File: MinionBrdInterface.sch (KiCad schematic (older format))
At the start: 8 parts, among them J7 MinionConn, U20 HX1188FNL, U5 LTC6820

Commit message: Lays out PCB for Controls leader board
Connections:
- net labels added: UART_Rx, UART_Tx
- net labels removed: UART2_Rx, UART2_Tx
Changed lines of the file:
@@
 $Descr A4 11693 8268
 encoding utf-8
-Sheet 10 11
+Sheet 10 10
 Title ""
 Date ""
@@
 Wire Wire Line
 	9750 3450 9400 3450
+Text Label 9400 3450 0    50   ~ 0
+UART_Rx
 Text Label 9400 3350 0    50   ~ 0
-UART2_Rx
-Text Label 9400 3450 0    50   ~ 0
-UART2_Tx
+UART_Tx
 Wire Wire Line
 	8350 3550 9750 3550
@@
 NoConn ~ 9750 4150
 NoConn ~ 9750 4250
-Text HLabel 9400 3350 0    50   Output ~ 0
-UART2_Rx
-Text HLabel 9400 3450 0    50   Input ~ 0
-UART2_Tx
+Text HLabel 9400 3450 0    50   Output ~ 0
+UART_Rx
+Text HLabel 9400 3350 0    50   Input ~ 0
+UART_Tx
+Text Label 2850 3700 0    50   ~ 0
+MOSI
+Text Label 2850 3800 0    50   ~ 0
+MISO
+Text Label 2850 3900 0    50   ~ 0
+CLK
+Text Label 2850 4000 0    50   ~ 0
+CS
 $EndSCHEMATC

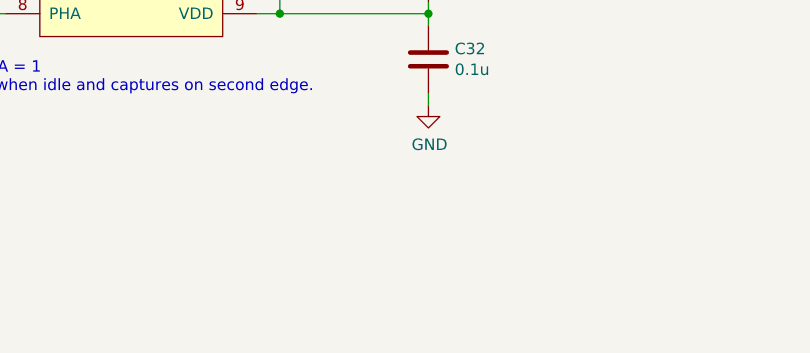
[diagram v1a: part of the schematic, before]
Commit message: Adds SPI header to test
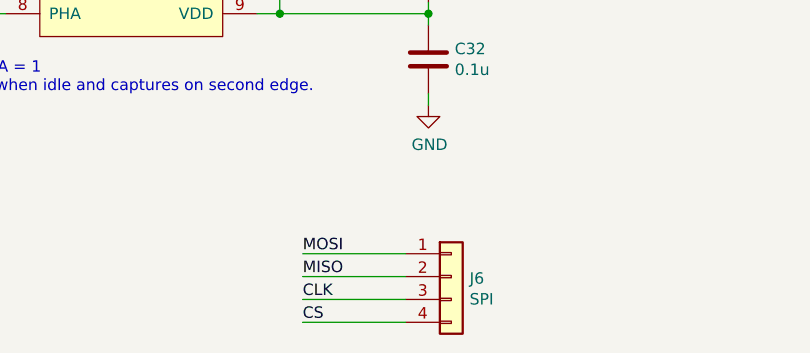
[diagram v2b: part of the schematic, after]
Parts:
- added J6: SPI, Connector_PinHeader_2.54mm:PinHeader_1x04_P2.54mm_Vertical, symbol Connector_Generic:Conn_01x04
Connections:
- wire segments 55 -> 59
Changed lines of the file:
@@
 Text Label 2850 4000 0    50   ~ 0
 CS
+$Comp
+L Connector_Generic:Conn_01x04 J6
+U 1 1 5F76763B
+P 5250 5450
+F 0 "J6" H 5330 5442 50  0000 L CNN
+F 1 "SPI" H 5330 5351 50  0000 L CNN
+F 2 "Connector_PinHeader_2.54mm:PinHeader_1x04_P2.54mm_Vertical" H 5250 5450 50  0001 C CNN
+F 3 "~" H 5250 5450 50  0001 C CNN
+	1    5250 5450
+	1    0    0    -1
+$EndComp
+Wire Wire Line
+	4600 5350 5050 5350
+Wire Wire Line
+	4600 5550 5050 5550
+Wire Wire Line
+	4600 5650 5050 5650
+Wire Wire Line
+	4600 5450 5050 5450
+Text Label 4600 5350 0    50   ~ 0
+MOSI
+Text Label 4600 5450 0    50   ~ 0
+MISO
+Text Label 4600 5550 0    50   ~ 0
+CLK
+Text Label 4600 5650 0    50   ~ 0
+CS
 $EndSCHEMATC

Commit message: Labels sections and fixes DRC errors
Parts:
- J7: footprint Connector_Molex:Molex_Micro-Fit_3.0_43650-1215_1x12_P3.00mm_Vertical -> UTSVT_Connectors:Molex_MicroFit3.0_2x6xP3.00mm_PolarizingPeg_Vertical; symbol Connector_Generic:Conn_01x12 -> Connector_Generic:Conn_02x06_Top_Bottom
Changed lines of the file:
@@
 Text Notes 2500 2650 0    50   ~ 0
 If the wires lengths are short and you want to save more power, change IBIAS\nresistor to be 2.8k. Look in LTC6820 datasheet for more information on\ncalculating these BIAS resistors.
-$Comp
-L Connector_Generic:Conn_01x12 J?
-U 1 1 5D76E59D
-P 9950 3650
-AR Path="/5C4C7509/5D76E59D" Ref="J?"  Part="1"
-AR Path="/5D766247/5D76E59D" Ref="J7"  Part="1"
-AR Path="/5F7B30EA/5D76E59D" Ref="J5"  Part="1"
-F 0 "J5" H 10029 3642 50  0000 L CNN
-F 1 "MinionConn" H 10029 3551 50  0000 L CNN
-F 2 "Connector_Molex:Molex_Micro-Fit_3.0_43650-1215_1x12_P3.00mm_Vertical" H 9950 3650 50  0001 C CNN
-F 3 "~" H 9950 3650 50  0001 C CNN
-	1    9950 3650
-	1    0    0    -1
-$EndComp
 Text Label 7150 3550 2    50   ~ 0
 IP
@@
 L power:+3.3V #PWR012
 U 1 1 5F8A5541
-P 9650 3100
-F 0 "#PWR012" H 9650 2950 50  0001 C CNN
-F 1 "+3.3V" H 9665 3273 50  0000 C CNN
-F 2 "" H 9650 3100 50  0001 C CNN
-F 3 "" H 9650 3100 50  0001 C CNN
-	1    9650 3100
+P 9550 3400
+F 0 "#PWR012" H 9550 3250 50  0001 C CNN
+F 1 "+3.3V" H 9565 3573 50  0000 C CNN
+F 2 "" H 9550 3400 50  0001 C CNN
+F 3 "" H 9550 3400 50  0001 C CNN
+	1    9550 3400
 	1    0    0    -1
 $EndComp
@@
 L power:+12V #PWR010
 U 1 1 5F8A5C41
-P 9400 3100
-F 0 "#PWR010" H 9400 2950 50  0001 C CNN
-F 1 "+12V" H 9415 3273 50  0000 C CNN
-F 2 "" H 9400 3100 50  0001 C CNN
-F 3 "" H 9400 3100 50  0001 C CNN
-	1    9400 3100
-	1    0    0    -1
-$EndComp
-Wire Wire Line
-	9750 3150 9650 3150
-Wire Wire Line
-	9650 3150 9650 3100
-Wire Wire Line
-	9750 3250 9400 3250
-Wire Wire Line
-	9400 3250 9400 3100
-Wire Wire Line
-	9750 3350 9400 3350
-Wire Wire Line
-	9750 3450 9400 3450
-Text Label 9400 3450 0    50   ~ 0
+P 10450 3400
+F 0 "#PWR010" H 10450 3250 50  0001 C CNN
+F 1 "+12V" H 10465 3573 50  0000 C CNN
+F 2 "" H 10450 3400 50  0001 C CNN
+F 3 "" H 10450 3400 50  0001 C CNN
+	1    10450 3400
+	-1   0    0    -1
+$EndComp
+Wire Wire Line
+	9750 3450 9550 3450
+Wire Wire Line
+	9550 3450 9550 3400
+Wire Wire Line
+	10450 3450 10450 3400
+Wire Wire Line
+	10250 3550 10600 3550
+Wire Wire Line
+	10250 3650 10600 3650
+Text Label 10600 3650 2    50   ~ 0
 UART_Rx
-Text Label 9400 3350 0    50   ~ 0
+Text Label 10600 3550 2    50   ~ 0
 UART_Tx
 Wire Wire Line
-	8350 3550 9750 3550
-Wire Wire Line
-	8750 3650 9750 3650
-Wire Wire Line
-	9750 3850 9600 3850
-Wire Wire Line
-	9600 3850 9600 3900
+	9750 3750 9550 3750
+Wire Wire Line
+	9550 3750 9550 3800
 $Comp
 L power:GND #PWR011
 U 1 1 5F8B0452
-P 9600 3900
-F 0 "#PWR011" H 9600 3650 50  0001 C CNN
-F 1 "GND" H 9605 3727 50  0000 C CNN
-F 2 "" H 9600 3900 50  0001 C CNN
-F 3 "" H 9600 3900 50  0001 C CNN
-	1    9600 3900
-	1    0    0    -1
-$EndComp
-$Comp
-L power:GNDPWR #PWR09
-U 1 1 5F8B0739
-P 9350 3900
-F 0 "#PWR09" H 9350 3700 50  0001 C CNN
-F 1 "GNDPWR" H 9354 3746 50  0000 C CNN
-F 2 "" H 9350 3850 50  0001 C CNN
-F 3 "" H 9350 3850 50  0001 C CNN
-	1    9350 3900
-	1    0    0    -1
-$EndComp
-Wire Wire Line
-	9350 3900 9350 3750
-Wire Wire Line
-	9350 3750 9750 3750
+P 9550 3800
+F 0 "#PWR011" H 9550 3550 50  0001 C CNN
+F 1 "GND" H 9555 3627 50  0000 C CNN
+F 2 "" H 9550 3800 50  0001 C CNN
+F 3 "" H 9550 3800 50  0001 C CNN
+	1    9550 3800
+	1    0    0    -1
+$EndComp
 NoConn ~ 9750 3950
-NoConn ~ 9750 4050
-NoConn ~ 9750 4150
-NoConn ~ 9750 4250
-Text HLabel 9400 3450 0    50   Output ~ 0
+NoConn ~ 9750 3850
+NoConn ~ 10250 3850
+NoConn ~ 10250 3950
+Text HLabel 10600 3650 2    50   Output ~ 0
 UART_Rx
-Text HLabel 9400 3350 0    50   Input ~ 0
+Text HLabel 10600 3550 2    50   Input ~ 0
 UART_Tx
 Text Label 2850 3700 0    50   ~ 0
@@
 Text Label 4600 5650 0    50   ~ 0
 CS
+$Comp
+L power:GNDPWR #PWR09
+U 1 1 5F8B0739
+P 10450 3800
+F 0 "#PWR09" H 10450 3600 50  0001 C CNN
+F 1 "GNDPWR" H 10454 3646 50  0000 C CNN
+F 2 "" H 10450 3750 50  0001 C CNN
+F 3 "" H 10450 3750 50  0001 C CNN
+	1    10450 3800
+	-1   0    0    -1
+$EndComp
+Wire Wire Line
+	10450 3750 10450 3800
+Wire Wire Line
+	8750 3650 9750 3650
+Wire Wire Line
+	8350 3550 9750 3550
+Wire Wire Line
+	10250 3450 10450 3450
+Wire Wire Line
+	10250 3750 10450 3750
+$Comp
+L Connector_Generic:Conn_02x06_Top_Bottom J?
+U 1 1 5D76E59D
+P 10050 3650
+AR Path="/5C4C7509/5D76E59D" Ref="J?"  Part="1"
+AR Path="/5D766247/5D76E59D" Ref="J7"  Part="1"
+AR Path="/5F7B30EA/5D76E59D" Ref="J5"  Part="1"
+F 0 "J5" H 10050 3250 50  0000 L CNN
+F 1 "MinionConn" H 9900 3150 50  0000 L CNN
+F 2 "UTSVT_Connectors:Molex_MicroFit3.0_2x6xP3.00mm_PolarizingPeg_Vertical" H 10050 3650 50  0001 C CNN
+F 3 "~" H 10050 3650 50  0001 C CNN
+	1    10050 3650
+	-1   0    0    -1
+$EndComp
 $EndSCHEMATC

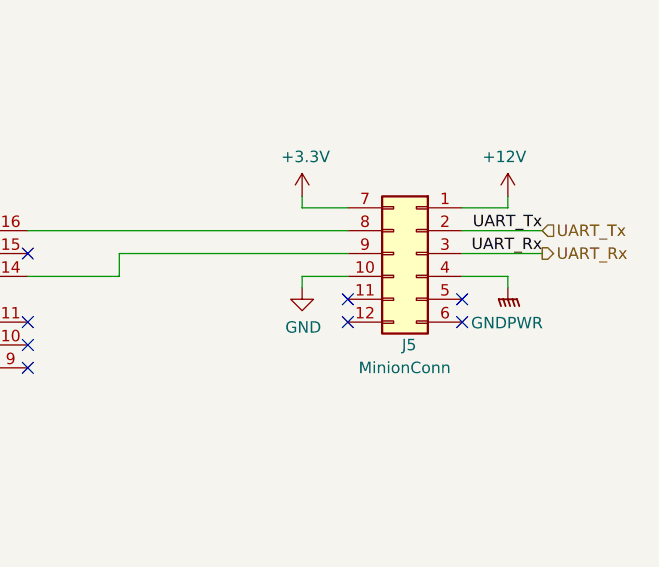
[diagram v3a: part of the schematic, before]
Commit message: Adds labels to some connectors and edits layout to meet 0,2mm pad to trace clearance
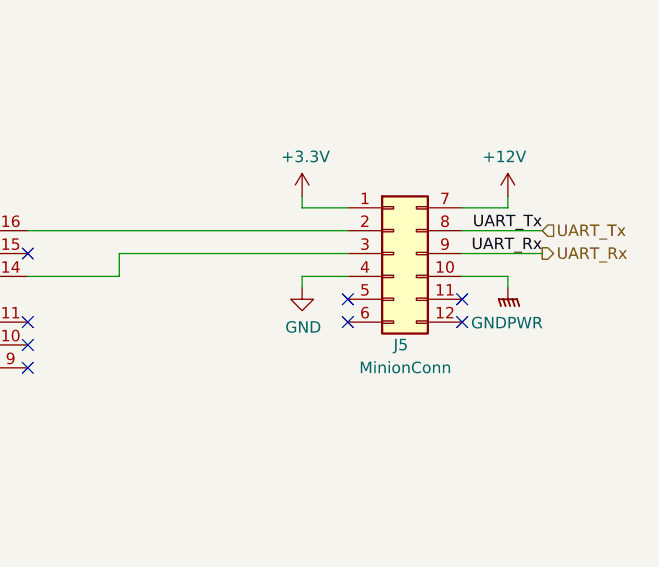
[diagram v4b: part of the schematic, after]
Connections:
- net +12V: now also J7.7 (Pin_7); no longer J7.1 (Pin_1)
- net +3V3: now also J7.1 (Pin_1); no longer J7.7 (Pin_7)
- net GND: now also J7.4 (Pin_4); no longer J7.10 (Pin_10)
- net GNDPWR: now also J7.10 (Pin_10); no longer J7.4 (Pin_4)
- net UART_Rx: now also J7.9 (Pin_9); no longer J7.3 (Pin_3)
- net UART_Tx: now also J7.8 (Pin_8); no longer J7.2 (Pin_2)
- net at U20.16 (TX+): now also J7.2 (Pin_2); no longer J7.8 (Pin_8)
- net at U20.14 (TX-): now also J7.3 (Pin_3); no longer J7.9 (Pin_9)
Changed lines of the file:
@@
 Wire Wire Line
 	10450 3450 10450 3400
-Wire Wire Line
-	10250 3550 10600 3550
-Wire Wire Line
-	10250 3650 10600 3650
 Text Label 10600 3650 2    50   ~ 0
 UART_Rx
@@
 	8350 3550 9750 3550
 Wire Wire Line
+	10250 3650 10600 3650
+Wire Wire Line
+	10250 3550 10600 3550
+Wire Wire Line
 	10250 3450 10450 3450
 Wire Wire Line
@@
 L Connector_Generic:Conn_02x06_Top_Bottom J?
 U 1 1 5D76E59D
-P 10050 3650
+P 9950 3650
 AR Path="/5C4C7509/5D76E59D" Ref="J?"  Part="1"
 AR Path="/5D766247/5D76E59D" Ref="J7"  Part="1"
 AR Path="/5F7B30EA/5D76E59D" Ref="J5"  Part="1"
-F 0 "J5" H 10050 3250 50  0000 L CNN
-F 1 "MinionConn" H 9900 3150 50  0000 L CNN
-F 2 "UTSVT_Connectors:Molex_MicroFit3.0_2x6xP3.00mm_PolarizingPeg_Vertical" H 10050 3650 50  0001 C CNN
-F 3 "~" H 10050 3650 50  0001 C CNN
-	1    10050 3650
-	-1   0    0    -1
+F 0 "J5" H 9950 3250 50  0000 L CNN
+F 1 "MinionConn" H 9800 3150 50  0000 L CNN
+F 2 "UTSVT_Connectors:Molex_MicroFit3.0_2x6xP3.00mm_PolarizingPeg_Vertical" H 9950 3650 50  0001 C CNN
+F 3 "~" H 9950 3650 50  0001 C CNN
+	1    9950 3650
+	1    0    0    -1
 $EndComp
 $EndSCHEMATC

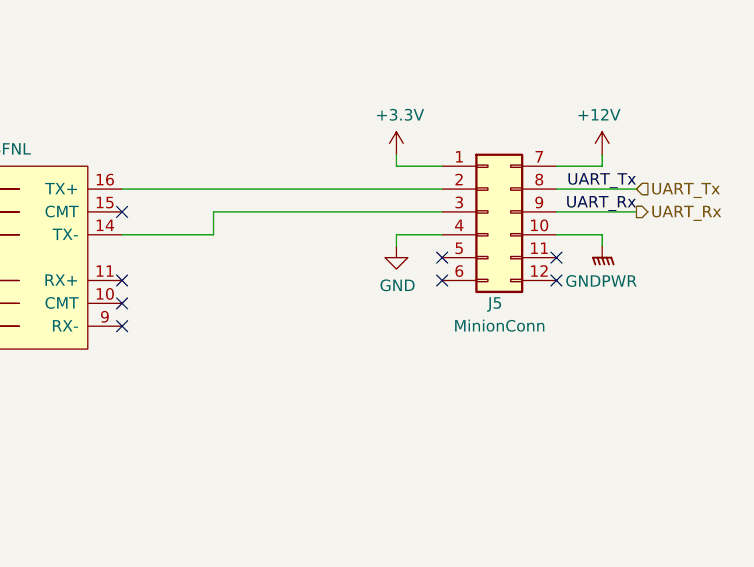
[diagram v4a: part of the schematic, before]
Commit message: Adds BPSPWR as a connection to the minion board and then fixes labels
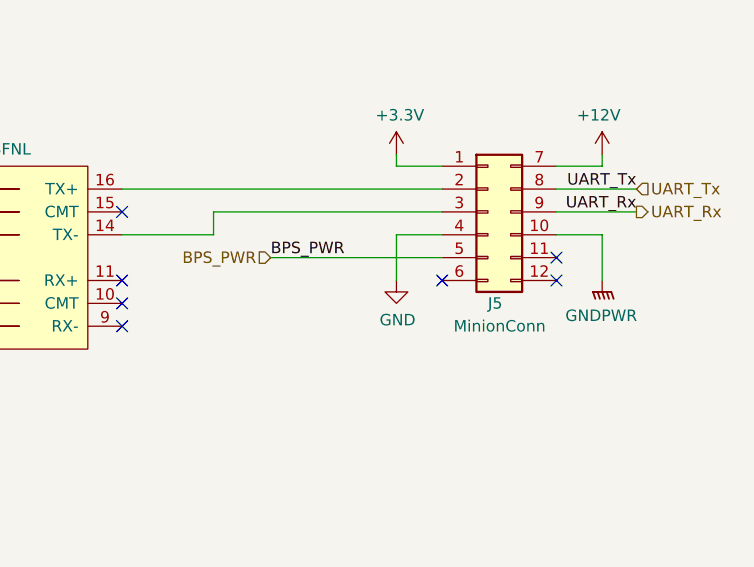
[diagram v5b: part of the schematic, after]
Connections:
- net BPS_PWR: now reaches J7.5 (Pin_5)
- no-connect marks 12 -> 11
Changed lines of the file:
@@
 UART_Tx
 Wire Wire Line
-	9750 3750 9550 3750
-Wire Wire Line
-	9550 3750 9550 3800
+	9550 3750 9550 3950
 $Comp
 L power:GND #PWR011
 U 1 1 5F8B0452
-P 9550 3800
-F 0 "#PWR011" H 9550 3550 50  0001 C CNN
-F 1 "GND" H 9555 3627 50  0000 C CNN
-F 2 "" H 9550 3800 50  0001 C CNN
-F 3 "" H 9550 3800 50  0001 C CNN
-	1    9550 3800
+P 9550 3950
+F 0 "#PWR011" H 9550 3700 50  0001 C CNN
+F 1 "GND" H 9555 3777 50  0000 C CNN
+F 2 "" H 9550 3950 50  0001 C CNN
+F 3 "" H 9550 3950 50  0001 C CNN
+	1    9550 3950
 	1    0    0    -1
 $EndComp
 NoConn ~ 9750 3950
-NoConn ~ 9750 3850
 NoConn ~ 10250 3850
 NoConn ~ 10250 3950
@@
 L power:GNDPWR #PWR09
 U 1 1 5F8B0739
-P 10450 3800
-F 0 "#PWR09" H 10450 3600 50  0001 C CNN
-F 1 "GNDPWR" H 10454 3646 50  0000 C CNN
-F 2 "" H 10450 3750 50  0001 C CNN
-F 3 "" H 10450 3750 50  0001 C CNN
-	1    10450 3800
+P 10450 3950
+F 0 "#PWR09" H 10450 3750 50  0001 C CNN
+F 1 "GNDPWR" H 10454 3796 50  0000 C CNN
+F 2 "" H 10450 3900 50  0001 C CNN
+F 3 "" H 10450 3900 50  0001 C CNN
+	1    10450 3950
 	-1   0    0    -1
 $EndComp
 Wire Wire Line
-	10450 3750 10450 3800
+	10450 3750 10450 3950
 Wire Wire Line
 	8750 3650 9750 3650
@@
 	1    0    0    -1
 $EndComp
+Text Label 9000 3850 0    50   ~ 0
+BPS_PWR
+Wire Wire Line
+	9000 3850 9750 3850
+Wire Wire Line
+	9750 3750 9550 3750
+Text HLabel 9000 3850 0    50   Input ~ 0
+BPS_PWR
 $EndSCHEMATC

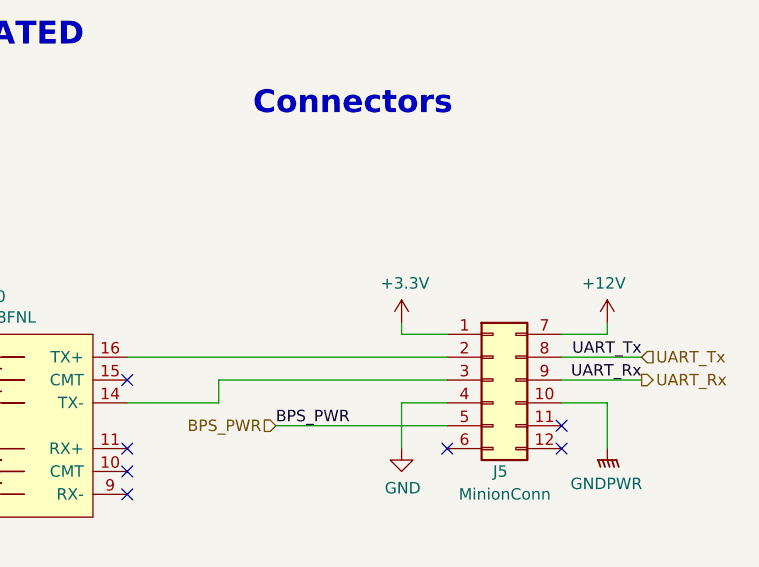
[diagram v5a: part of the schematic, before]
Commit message: Changes display power to 5V, puts fault LED on back, and adds gerbers
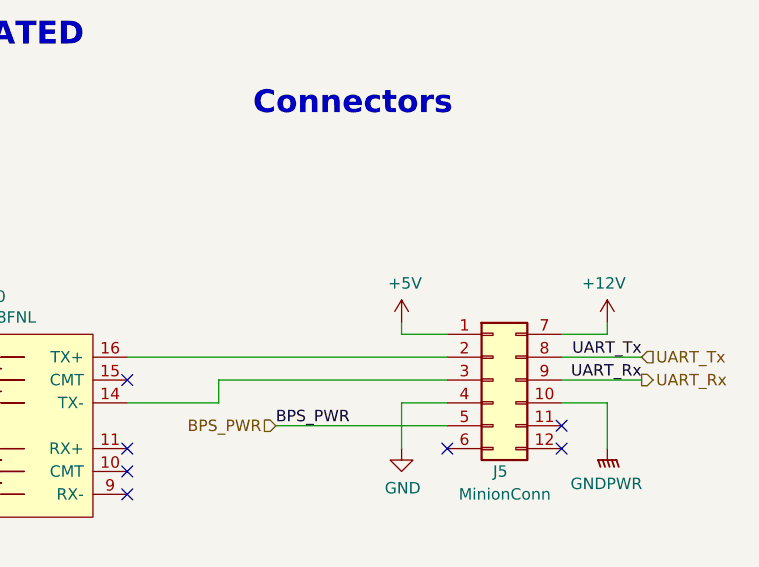
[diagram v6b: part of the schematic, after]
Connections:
- net +3V3: no longer J7.1 (Pin_1)
- net +5V: now also J7.1 (Pin_1)
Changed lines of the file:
@@
 NoConn ~ 7150 4150
-$Comp
-L power:+3.3V #PWR012
-U 1 1 5F8A5541
-P 9550 3400
-F 0 "#PWR012" H 9550 3250 50  0001 C CNN
-F 1 "+3.3V" H 9565 3573 50  0000 C CNN
-F 2 "" H 9550 3400 50  0001 C CNN
-F 3 "" H 9550 3400 50  0001 C CNN
-	1    9550 3400
-	1    0    0    -1
-$EndComp
 $Comp
 L power:+12V #PWR010
@@
 Text HLabel 9000 3850 0    50   Input ~ 0
 BPS_PWR
+$Comp
+L power:+5V #PWR?
+U 1 1 5FFC4650
+P 9550 3400
+F 0 "#PWR?" H 9550 3250 50  0001 C CNN
+F 1 "+5V" H 9565 3573 50  0000 C CNN
+F 2 "" H 9550 3400 50  0001 C CNN
+F 3 "" H 9550 3400 50  0001 C CNN
+	1    9550 3400
+	1    0    0    -1
+$EndComp
 $EndSCHEMATC

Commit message: USB Tx/Rx, Crystal Keepout, 12V Separation, Can2-Can3, Motor CAN bus labels, Power Input Protection Circuitry
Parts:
- U5: symbol utsvt-bps:LTC6820 -> Dashboard-rescue:LTC6820-utsvt-bps
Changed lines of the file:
@@
 	8350 3750 8750 3750
 $Comp
-L utsvt-bps:LTC6820 U?
+L Dashboard-rescue:LTC6820-utsvt-bps U?
 U 1 1 5F13EA7A
 P 3850 3500
@@
 BPS_PWR
 $Comp
-L power:+5V #PWR?
+L power:+5V #PWR0130
 U 1 1 5FFC4650
 P 9550 3400
-F 0 "#PWR?" H 9550 3250 50  0001 C CNN
+F 0 "#PWR0130" H 9550 3250 50  0001 C CNN
 F 1 "+5V" H 9565 3573 50  0000 C CNN
 F 2 "" H 9550 3400 50  0001 C CNN

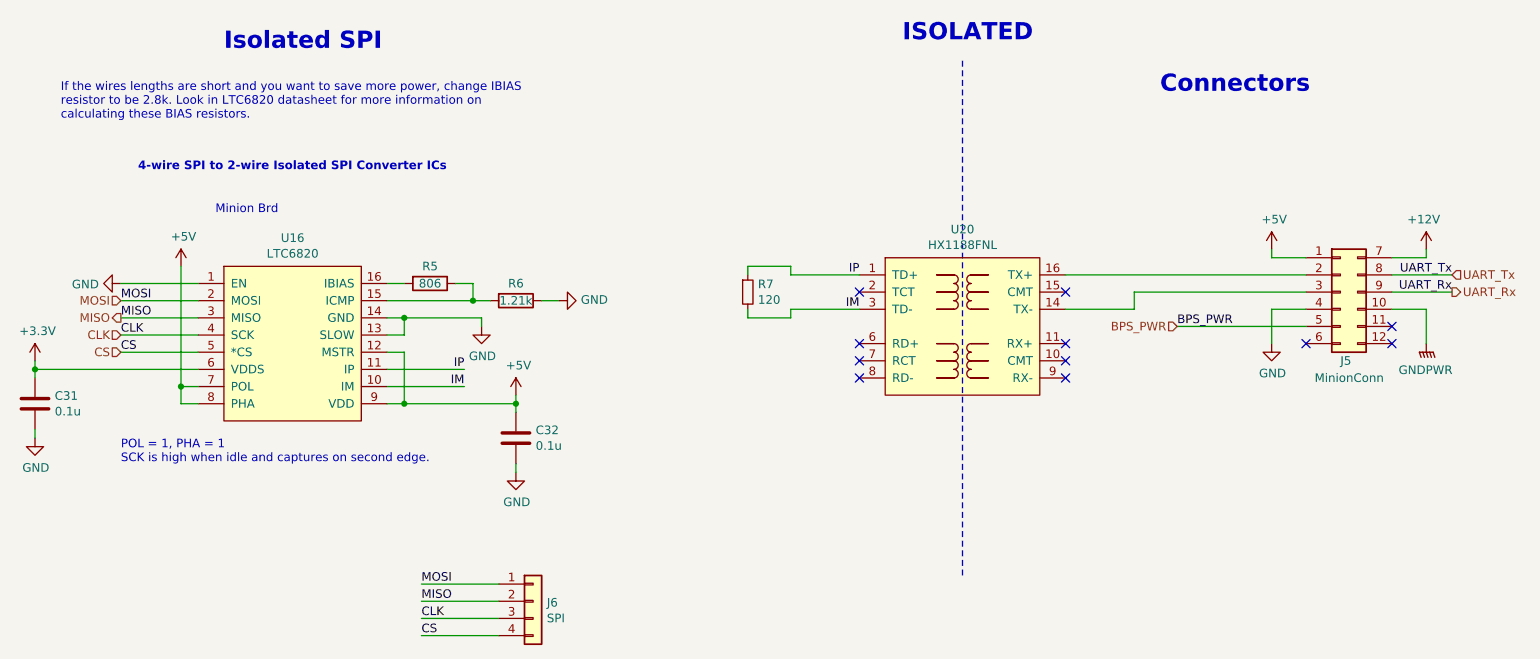
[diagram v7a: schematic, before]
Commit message: removes the isp
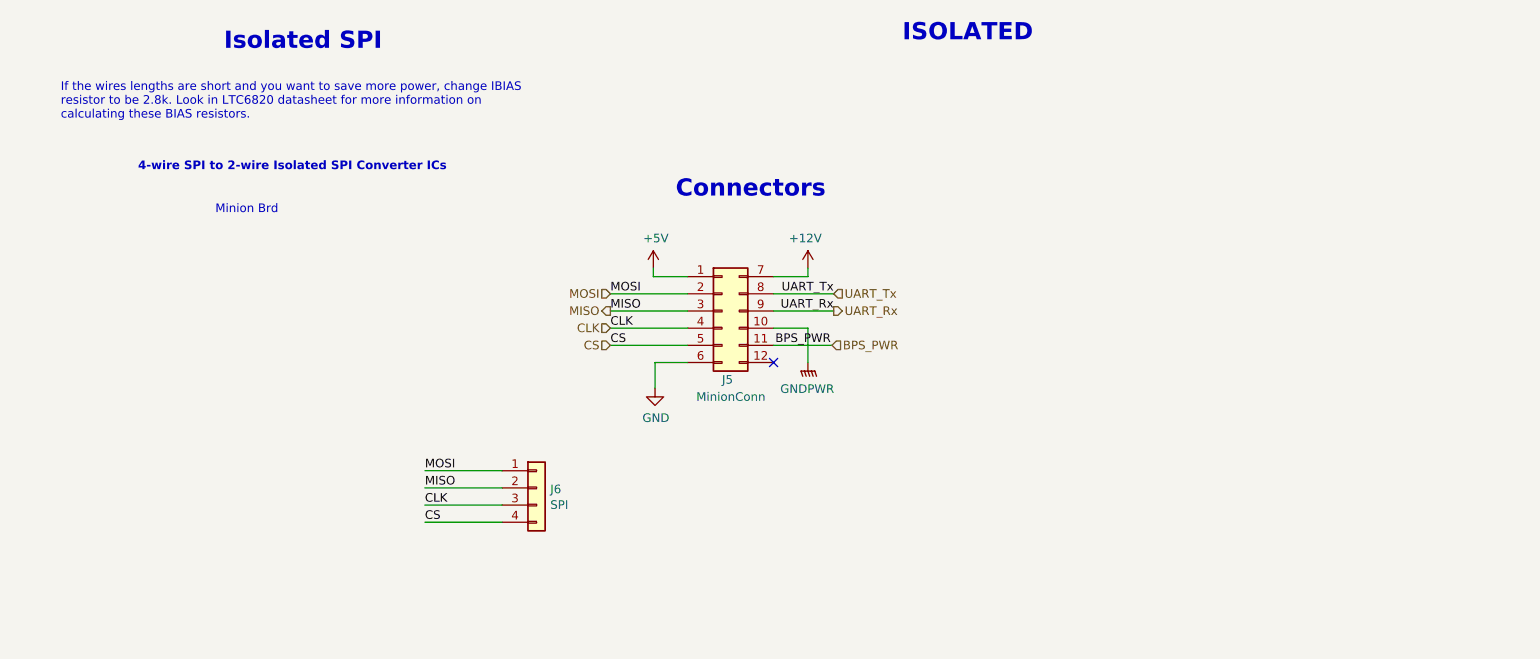
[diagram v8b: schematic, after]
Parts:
- removed C16, C18: 0.1u, Capacitor_SMD:C_0805_2012Metric, symbol Device:C
- removed R13: 806, Resistor_SMD:R_0805_2012Metric, symbol Device:R
- removed R15: 1.21k, Resistor_SMD:R_0805_2012Metric, symbol Device:R
- removed R17: 120, Resistor_SMD:R_0805_2012Metric, symbol Device:R_Small
- removed U20: HX1188FNL, UTSVT_Passive:HXXXX, symbol utsvt-chips:HX1188FNL
- removed U5: LTC6820, Package_SO:MSOP-16_3x4mm_P0.5mm, symbol Dashboard-rescue:LTC6820-utsvt-bps
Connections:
- net BPS_PWR: now also J7.11 (Pin_11); no longer J7.5 (Pin_5)
- net CLK: now also J7.4 (Pin_4)
- net CS: now also J7.5 (Pin_5)
- net GND: now also J7.6 (Pin_6); no longer J7.4 (Pin_4)
- net MISO: now also J7.3 (Pin_3)
- net MOSI: now also J7.2 (Pin_2)
- no-connect marks 11 -> 1
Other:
- note removed: "POL = 1, PHA = 1\nSCK is high when idle and captures on second edge."
- moved on the sheet: J5, J6
